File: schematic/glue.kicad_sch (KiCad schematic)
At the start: 9 parts, among them J6 Conn_02x05_Odd_Even, U9 EPM7064SLC

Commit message: bootup works, controller waits, but no response
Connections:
- net C1P4 is gone; now on net C1P5: U9.8 (I/O)
- net C2P4 is gone; now on net C2P5: U9.76 (I/O)
- net C1P5: no longer U9.9 (I/O)
- net C1P6: now also U9.9 (I/O); no longer U9.10 (I/O)
- net C1P8: now also U9.10 (I/O); no longer U9.12 (I/O)
- net C2P5: no longer U9.77 (I/O)
- net C2P6: now also U9.77 (I/O); no longer U9.79 (I/O)
- net C2P8: now also U9.79 (I/O); no longer U9.81 (I/O)
- net C1P7 renamed C4_ARM
- net C2P7 renamed RX
- new net C7_FIRE: U9.12 (I/O)
- new net TX: U9.81 (I/O)

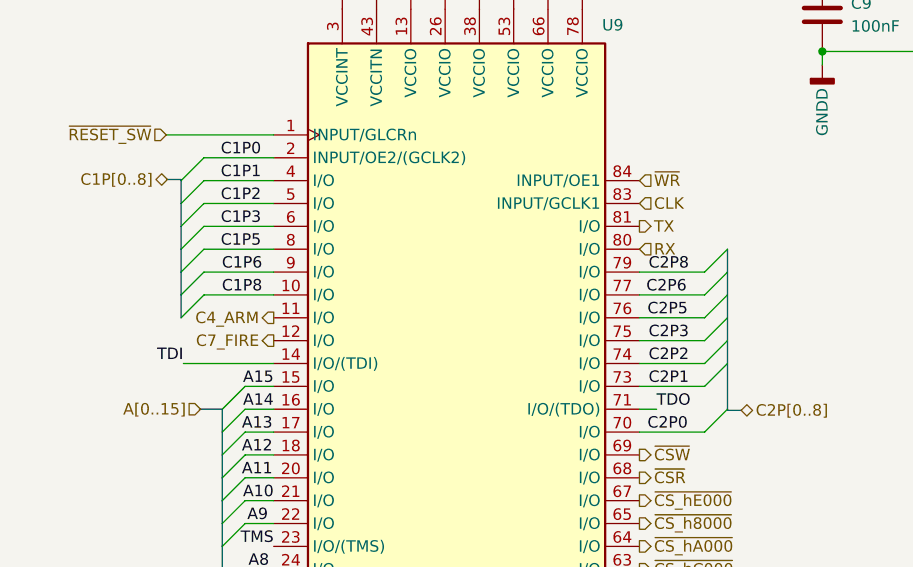
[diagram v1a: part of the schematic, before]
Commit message: added volume and adjusted cart port
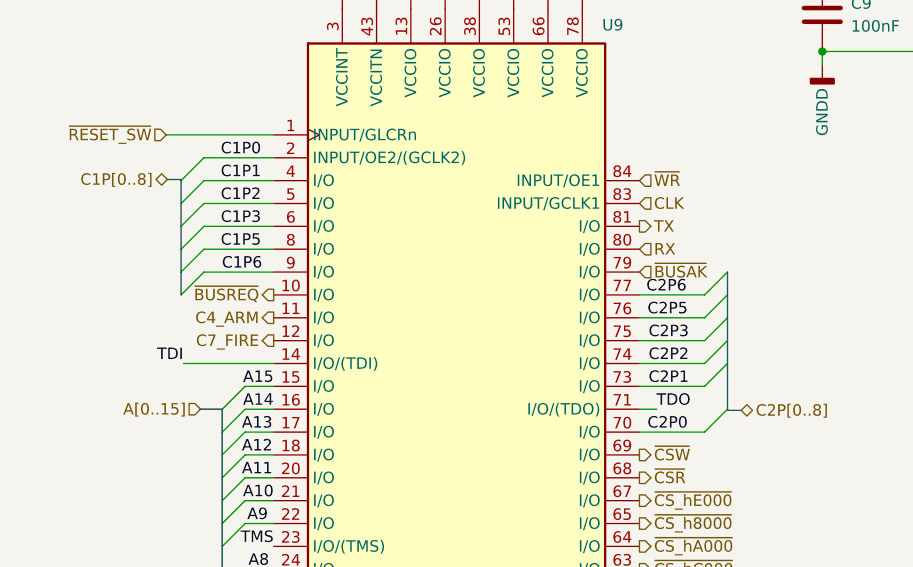
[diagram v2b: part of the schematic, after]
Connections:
- net C1P8 renamed ~{BUSREQ}
- net C2P8 renamed ~{BUSAK}
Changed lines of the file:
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@@
-    (stroke (width 0) (type default))
-  )
-  (bus_entry (at 131.826 70.612) (size -2.54 2.54)
     (stroke (width 0) (type default))
   )
@@
     (stroke (width 0) (type default))
   )
-  (bus_entry (at 71.12 78.232) (size 2.54 -2.54)
-    (stroke (width 0) (type default))
-  )
   (bus_entry (at 75.692 118.872) (size 2.54 -2.54)
     (stroke (width 0) (type default))
@@
     (stroke (width 0) (type default))
   )
-  (wire (pts (xy 73.66 75.692) (xy 81.407 75.692))
-    (stroke (width 0) (type default))
-  )
   (bus (pts (xy 73.152 88.392) (xy 75.692 88.392))
     (stroke (width 0) (type default))
@@
     (stroke (width 0) (type default))
   )
-  (bus (pts (xy 71.12 75.692) (xy 71.12 78.232))
-    (stroke (width 0) (type default))
-  )
   (wire (pts (xy 124.079 145.796) (xy 124.079 144.272))
     (stroke (width 0) (type default))
@@
     (stroke (width 0) (type default))
   )
-  (bus (pts (xy 131.826 70.612) (xy 131.826 73.152))
-    (stroke (width 0) (type default))
-  )
   (wire (pts (xy 123.952 134.112) (xy 122.047 134.112))
     (stroke (width 0) (type default))
@@
     (stroke (width 0) (type default))
   )
-  (wire (pts (xy 122.047 73.152) (xy 129.286 73.152))
-    (stroke (width 0) (type default))
-  )
   (bus (pts (xy 131.826 83.312) (xy 131.826 80.772))
     (stroke (width 0) (type default))
@@
     (effects (font (size 1.27 1.27)) (justify left bottom))
   )
-  (label "C1P8" (at 80.137 75.692 180) (fields_autoplaced)
-    (effects (font (size 1.27 1.27)) (justify right bottom))
-  )
   (label "C1P0" (at 80.01 60.452 180) (fields_autoplaced)
     (effects (font (size 1.27 1.27)) (justify right bottom))
@@
     (effects (font (size 1.27 1.27)) (justify right bottom))
   )
-  (label "C2P8" (at 123.063 73.152 0) (fields_autoplaced)
-    (effects (font (size 1.27 1.27)) (justify left bottom))
-  )
   (label "A8" (at 80.899 106.172 180) (fields_autoplaced)
     (effects (font (size 1.27 1.27)) (justify right bottom))
@@
     (effects (font (size 1.27 1.27)) (justify right))
   )
+  (hierarchical_label "~{BUSAK}" (shape input) (at 122.047 73.152 0) (fields_autoplaced)
+    (effects (font (size 1.27 1.27)) (justify left))
+  )
   (hierarchical_label "CLK" (shape input) (at 122.047 65.532 0) (fields_autoplaced)
     (effects (font (size 1.27 1.27)) (justify left))
@@
     (effects (font (size 1.27 1.27)) (justify left))
   )
+  (hierarchical_label "~{BUSREQ}" (shape output) (at 81.407 75.692 180) (fields_autoplaced)
+    (effects (font (size 1.27 1.27)) (justify right))
+  )
   (hierarchical_label "~{WAIT}" (shape output) (at 65.659 136.652 180) (fields_autoplaced)

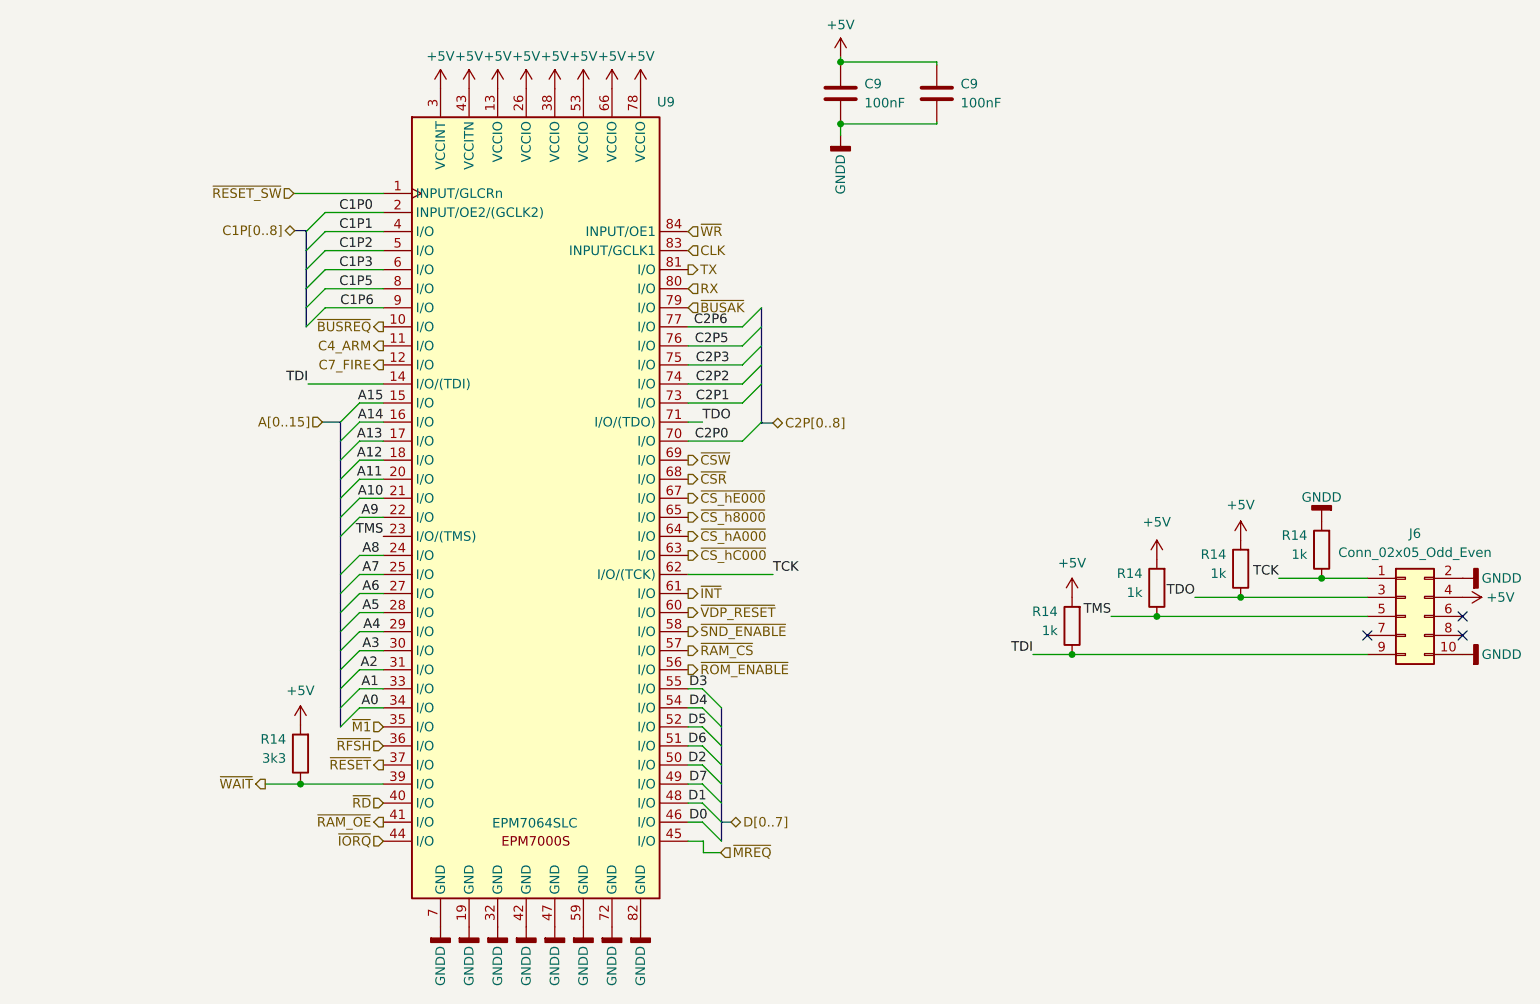
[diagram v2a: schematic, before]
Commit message: first version with roller controller compat
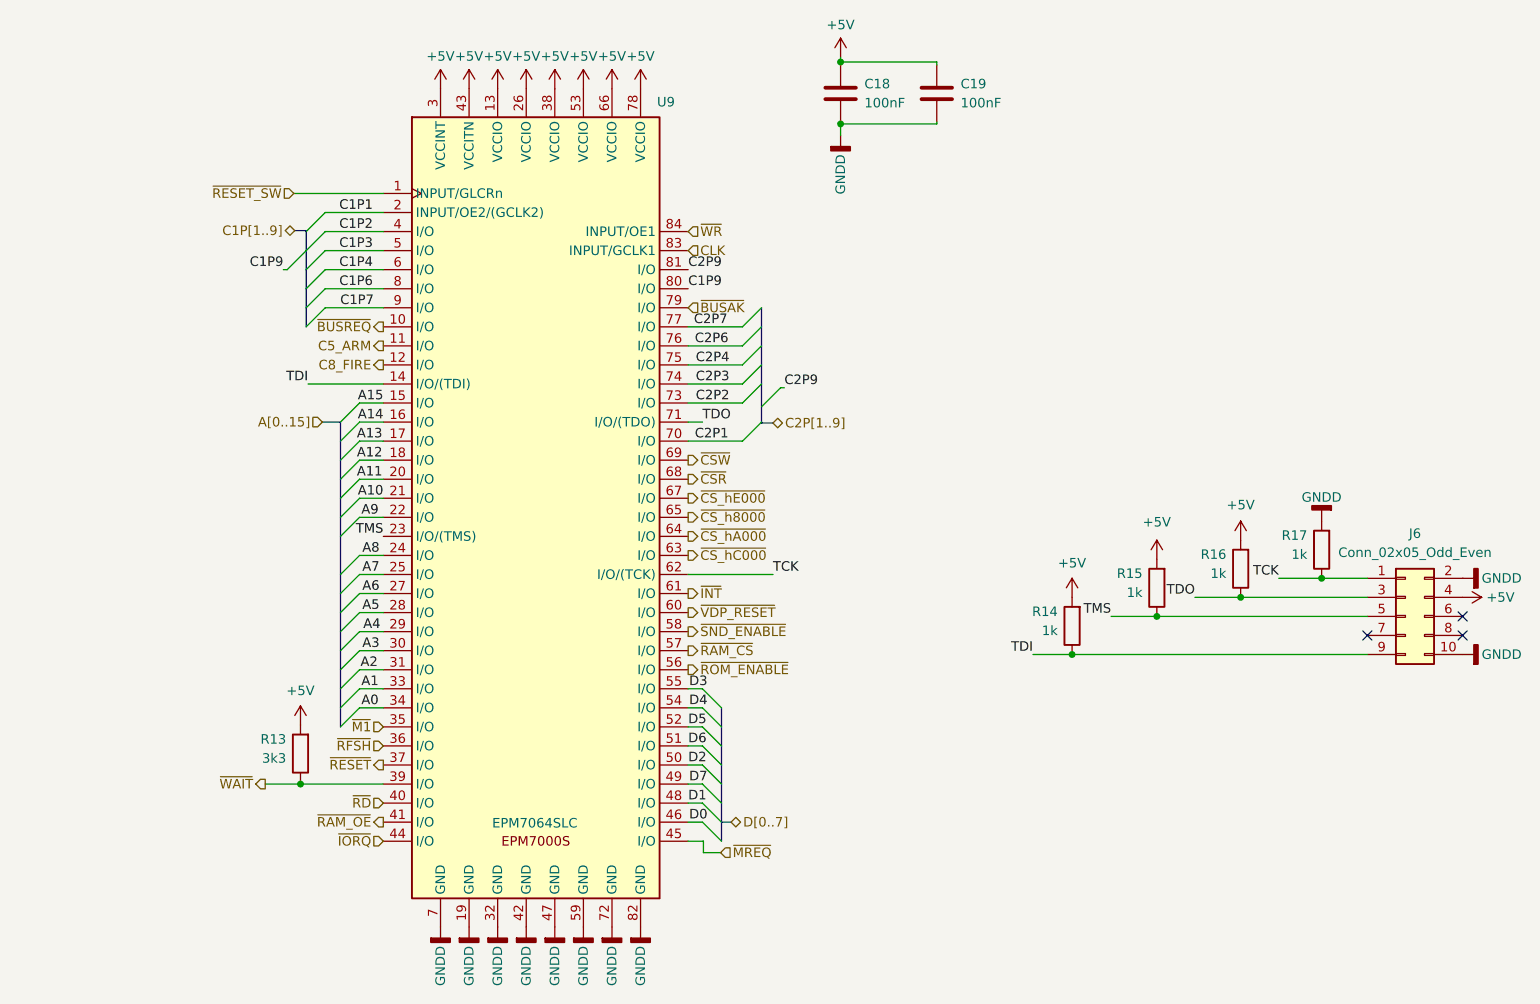
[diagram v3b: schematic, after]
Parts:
- renumbered C9 to C18, C9 to C19, R14 to R13, R14 to R15, R14 to R16, R14 to R17
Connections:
- net C1P0 is gone; now on net C1P1: U9.2 (INPUT/OE2/(GCLK2))
- net C1P5 is gone; now on net C1P6: U9.8 (I/O)
- net C2P0 is gone; now on net C2P1: U9.70 (I/O)
- net C2P5 is gone; now on net C2P6: U9.76 (I/O)
- net C1P1: no longer U9.4 (I/O)
- net C1P2: now also U9.4 (I/O); no longer U9.5 (I/O)
- net C1P3: now also U9.5 (I/O); no longer U9.6 (I/O)
- net C1P6: no longer U9.9 (I/O)
- net C2P1: no longer U9.73 (I/O)
- net C2P2: now also U9.73 (I/O); no longer U9.74 (I/O)
- net C2P3: now also U9.74 (I/O); no longer U9.75 (I/O)
- net C2P6: no longer U9.77 (I/O)
- net C4_ARM renamed C5_ARM
- net C7_FIRE renamed C8_FIRE
- net RX renamed C1P9
- net TX renamed C2P9
- new net C1P4: U9.6 (I/O)
- new net C1P7: U9.9 (I/O)
- new net C2P4: U9.75 (I/O)
- new net C2P7: U9.77 (I/O)

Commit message: update pdf schematic and schematic wording
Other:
- company: (none) -> sparkletron
- title: (none) -> Mini Colecovision
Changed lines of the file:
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@@
 (kicad_sch (version 20230121) (generator eeschema)
-  (paper "A4")
+  (paper "USLetter")
+  (title_block
+    (title "Mini Colecovision")
+    (date "2024-03-25")
+    (rev "1.0.0")
+    (company "sparkletron")
+    (comment 1 "Jay Convertino")
+    (comment 2 "MIT LICENSE")
+    (comment 3 "TARGET: Portable")
+  )
   (junction (at 173.228 119.38) (diameter 0) (color 0 0 0 0)
   )

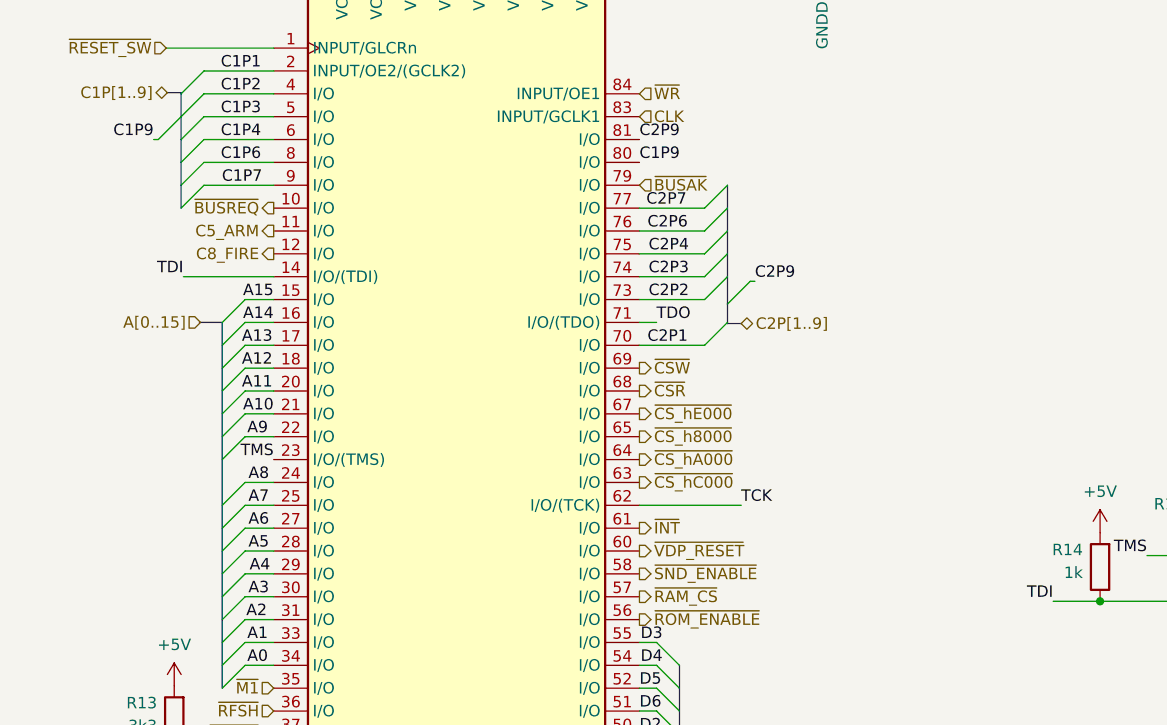
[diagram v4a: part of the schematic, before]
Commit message: first commit with PCB revised for super game module. Needs model updates and tweaks
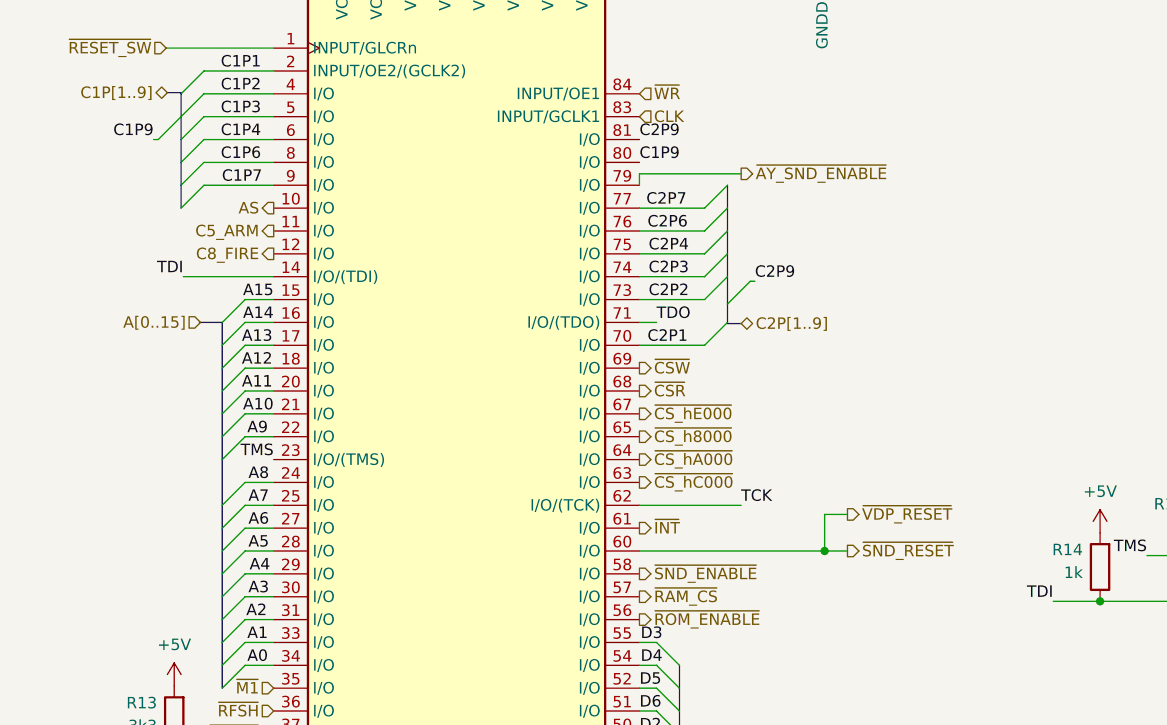
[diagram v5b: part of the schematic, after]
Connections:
- net ~{BUSAK} renamed ~{AY_SND_ENABLE}
- net ~{BUSREQ} renamed AS
- net ~{VDP_RESET} renamed ~{SND_RESET}
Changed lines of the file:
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@@
   (junction (at 142.367 40.386) (diameter 0) (color 0 0 0 0)
+  )
+  (junction (at 142.621 113.792) (diameter 0) (color 0 0 0 0)
   )
   (no_connect (at 225.298 114.3))
@@
     (stroke (width 0) (type default))
   )
+  (wire (pts (xy 145.161 113.792) (xy 142.621 113.792))
+    (stroke (width 0) (type default))
+  )
   (wire (pts (xy 123.952 123.952) (xy 122.047 123.952))
     (stroke (width 0) (type default))
@@
     (stroke (width 0) (type default))
   )
+  (wire (pts (xy 142.494 113.792) (xy 122.047 113.792))
+    (stroke (width 0) (type default))
+  )
   (bus (pts (xy 69.596 62.865) (xy 71.12 62.865))
     (stroke (width 0) (type default))
@@
     (stroke (width 0) (type default))
   )
+  (wire (pts (xy 142.621 113.792) (xy 142.621 113.919))
+    (stroke (width 0) (type default))
+  )
   (bus (pts (xy 75.692 111.252) (xy 75.692 113.792))
     (stroke (width 0) (type default))
@@
     (stroke (width 0) (type default))
   )
+  (wire (pts (xy 145.161 109.728) (xy 142.621 109.728))
+    (stroke (width 0) (type default))
+  )
   (wire (pts (xy 78.232 123.952) (xy 81.407 123.952))
     (stroke (width 0) (type default))
@@
     (stroke (width 0) (type default))
   )
+  (wire (pts (xy 122.047 71.882) (xy 122.047 73.152))
+    (stroke (width 0) (type default))
+  )
   (bus (pts (xy 131.826 86.36) (xy 131.826 88.392))
     (stroke (width 0) (type default))
@@
     (stroke (width 0) (type default))
   )
+  (wire (pts (xy 142.494 113.919) (xy 142.494 113.792))
+    (stroke (width 0) (type default))
+  )
   (wire (pts (xy 122.047 83.312) (xy 129.286 83.312))
     (stroke (width 0) (type default))
@@
     (stroke (width 0) (type default))
   )
+  (wire (pts (xy 133.35 71.882) (xy 122.047 71.882))
+    (stroke (width 0) (type default))
+  )
   (bus (pts (xy 126.492 129.032) (xy 126.492 126.492))
     (stroke (width 0) (type default))
@@
     (stroke (width 0) (type default))
   )
+  (wire (pts (xy 142.621 109.728) (xy 142.621 113.792))
+    (stroke (width 0) (type default))
+  )
+  (wire (pts (xy 142.621 113.919) (xy 142.494 113.919))
+    (stroke (width 0) (type default))
+  )
   (bus (pts (xy 131.826 83.312) (xy 131.826 86.36))
     (stroke (width 0) (type default))
@@
     (effects (font (size 1.27 1.27)) (justify right))
   )
-  (hierarchical_label "~{BUSAK}" (shape input) (at 122.047 73.152 0) (fields_autoplaced)
+  (hierarchical_label "~{AY_SND_ENABLE}" (shape output) (at 133.35 71.882 0) (fields_autoplaced)
     (effects (font (size 1.27 1.27)) (justify left))
   )
@@
     (effects (font (size 1.27 1.27)) (justify left))
   )
-  (hierarchical_label "~{BUSREQ}" (shape output) (at 81.407 75.692 180) (fields_autoplaced)
+  (hierarchical_label "AS" (shape output) (at 81.407 75.692 180) (fields_autoplaced)
     (effects (font (size 1.27 1.27)) (justify right))
   )
@@
     (effects (font (size 1.27 1.27)) (justify left))
   )
-  (hierarchical_label "~{VDP_RESET}" (shape output) (at 122.047 113.792 0) (fields_autoplaced)
-    (effects (font (size 1.27 1.27)) (justify left))
-  )
+  (hierarchical_label "~{SND_RESET}" (shape output) (at 145.161 113.792 0) (fields_autoplaced)
+    (effects (font (size 1.27 1.27)) (justify left))
+  )
+  (hierarchical_label "~{VDP_RESET}" (shape output) (at 145.161 109.728 0) (fields_autoplaced)
+    (effects (font (size 1.27 1.27)) (justify left))
+  )

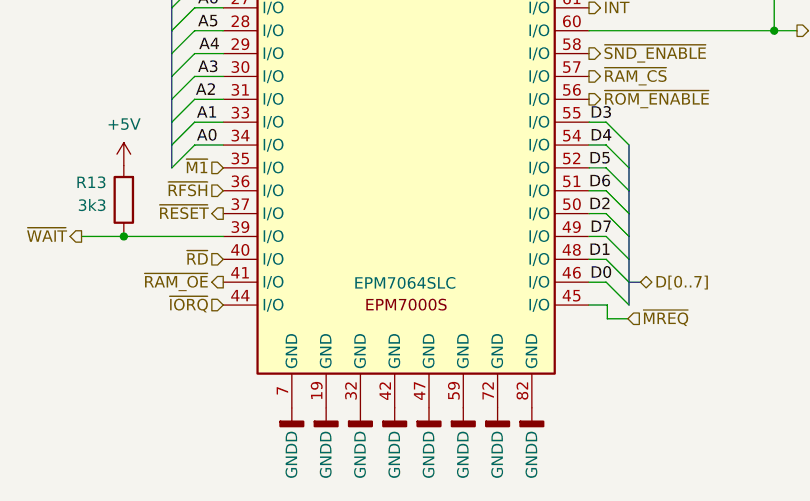
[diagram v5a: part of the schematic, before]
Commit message: update cpld to 7128 in schematic
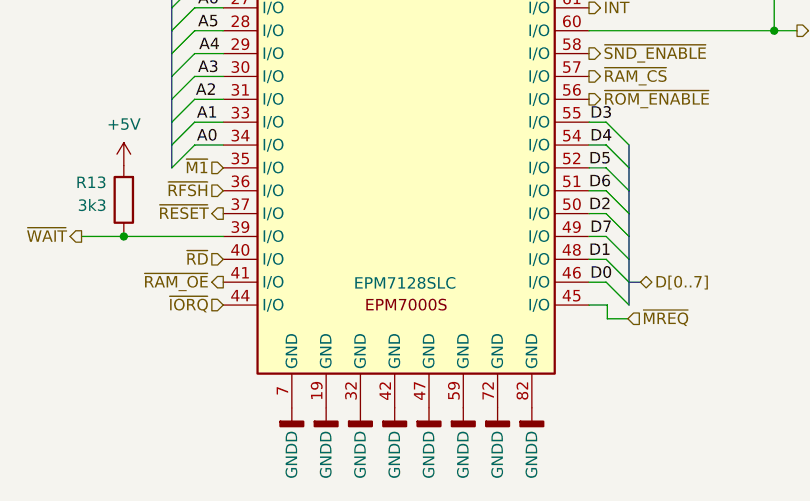
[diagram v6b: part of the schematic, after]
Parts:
- U9: value EPM7064SLC -> EPM7128SLC
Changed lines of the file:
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@@
       (effects (font (size 1.27 1.27)) (justify left))
     )
-    (property "Value" "EPM7064SLC" (at 101.6 141.859 0)
+    (property "Value" "EPM7128SLC" (at 101.6 141.859 0)
       (effects (font (size 1.27 1.27)))
     )
